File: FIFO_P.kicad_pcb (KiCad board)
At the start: 4 copper layers, 100 x 100 mm, 77 parts, among them J1 Vin +, J2 Vin -, J3 ICLK, J4 Vout, J5 Jack-DC, M3 MountingHole_3.2mm_M3_ISO14580, M4 MountingHole_4.3mm_M4_Pad_Via, SW1 Rotary_Encoder_61C, U1 SN74LVC2G157_MUX_TI, U10 AD7840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

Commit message: Fixed FIFO pin
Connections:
- U5 pad 13: GND -> (no net)
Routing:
- net (no net): track 0.00 -> 8.72 mm
- net GND: track 79.1 -> 77.0 mm, vias 11 -> 10
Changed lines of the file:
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@@
     (thickness 1.6)
     (drawings 116)
-    (tracks 1157)
+    (tracks 1160)
     (zones 0)
     (modules 77)
@@
     (mod_text_size 1 1)
     (mod_text_width 0.15)
-    (pad_size 3 3)
-    (pad_drill 1.52)
+    (pad_size 2.25 0.55)
+    (pad_drill 0)
     (pad_to_mask_clearance 0)
     (aux_axis_origin 0 0)
@@
     (pad 12 smd roundrect (at -8.05 2.8 270) (size 2.25 0.55) (layers F.Cu F.Paste F.Mask) (roundrect_rratio 0.25)
       (net 33 "Net-(U3-Pad20)"))
-    (pad 13 smd roundrect (at -8.05 3.6 270) (size 2.25 0.55) (layers F.Cu F.Paste F.Mask) (roundrect_rratio 0.25)
-      (net 88 GND))
+    (pad 13 smd roundrect (at -8.05 3.6 270) (size 2.25 0.55) (layers F.Cu F.Paste F.Mask) (roundrect_rratio 0.25))
     (pad 14 smd roundrect (at -8.05 4.4 270) (size 2.25 0.55) (layers F.Cu F.Paste F.Mask) (roundrect_rratio 0.25)
       (net 36 "Net-(U3-Pad17)"))
@@
   (gr_line (start 149.5 49.5) (end 149.5 149.5) (layer Edge.Cuts) (width 0.1))
   (gr_line (start 49.5 49.5) (end 149.5 49.5) (layer Edge.Cuts) (width 0.1))
+  (segment (start 113.1318 82.0414) (end 112.95001 82.22319) (width 0.25) (layer F.Cu) (net 0))
+  (segment (start 114.2568 82.0414) (end 113.1318 82.0414) (width 0.25) (layer F.Cu) (net 0))
+  (segment (start 112.95001 82.22319) (end 112.95001 86.45001) (width 0.25) (layer F.Cu) (net 0))
+  (segment (start 112.95001 86.45001) (end 114 87.5) (width 0.25) (layer F.Cu) (net 0))
+  (segment (start 114 87.5) (end 114 89.125) (width 0.25) (layer F.Cu) (net 0))
   (segment (start 115.3818 72.2914) (end 116.75 70.9232) (width 0.25) (layer F.Cu) (net 1))
   (segment (start 114.2568 72.2914) (end 115.3818 72.2914) (width 0.25) (layer F.Cu) (net 1))
@@
   (segment (start 114.8 87.387538) (end 114.8 87.9) (width 0.25) (layer F.Cu) (net 33))
   (segment (start 116.756064 82.799934) (end 115.415 84.140998) (width 0.25) (layer F.Cu) (net 33))
-  (segment (start 114.2568 80.0914) (end 113.1318 80.0914) (width 0.25) (layer F.Cu) (net 34))
-  (segment (start 111.849978 87.650022) (end 111.6 87.9) (width 0.25) (layer F.Cu) (net 34))
   (segment (start 111.6 87.9) (end 111.6 89.125) (width 0.25) (layer F.Cu) (net 34))
-  (segment (start 111.849978 81.373222) (end 111.849978 87.650022) (width 0.25) (layer F.Cu) (net 34))
-  (segment (start 113.1318 80.0914) (end 111.849978 81.373222) (width 0.25) (layer F.Cu) (net 34))
-  (segment (start 112.299989 87.799989) (end 112.299989 81.573211) (width 0.25) (layer F.Cu) (net 35))
-  (segment (start 112.299989 81.573211) (end 113.1318 80.7414) (width 0.25) (layer F.Cu) (net 35))
+  (segment (start 114.2568 80.0914) (end 113.1318 80.0914) (width 0.25) (layer F.Cu) (net 34))
+  (segment (start 111.599978 87.899978) (end 111.6 87.9) (width 0.25) (layer F.Cu) (net 34))
+  (segment (start 111.599978 81.623222) (end 111.599978 87.899978) (width 0.25) (layer F.Cu) (net 34))
+  (segment (start 113.1318 80.0914) (end 111.599978 81.623222) (width 0.25) (layer F.Cu) (net 34))
   (segment (start 113.1318 80.7414) (end 114.2568 80.7414) (width 0.25) (layer F.Cu) (net 35))
-  (segment (start 112.4 87.9) (end 112.299989 87.799989) (width 0.25) (layer F.Cu) (net 35))
-  (segment (start 112.4 89.125) (end 112.4 87.9) (width 0.25) (layer F.Cu) (net 35))
-  (segment (start 112.75 81.7732) (end 112.75 87.45) (width 0.25) (layer F.Cu) (net 36))
-  (segment (start 113.1318 81.3914) (end 112.75 81.7732) (width 0.25) (layer F.Cu) (net 36))
-  (segment (start 114.2568 81.3914) (end 113.1318 81.3914) (width 0.25) (layer F.Cu) (net 36))
-  (segment (start 112.75 87.45) (end 113.2 87.9) (width 0.25) (layer F.Cu) (net 36))
+  (segment (start 112.4 87.736411) (end 112.049989 87.3864) (width 0.25) (layer F.Cu) (net 35))
+  (segment (start 112.049989 81.823211) (end 113.1318 80.7414) (width 0.25) (layer F.Cu) (net 35))
+  (segment (start 112.4 89.125) (end 112.4 87.736411) (width 0.25) (layer F.Cu) (net 35))
+  (segment (start 112.049989 87.3864) (end 112.049989 81.823211) (width 0.25) (layer F.Cu) (net 35))
   (segment (start 113.2 87.9) (end 113.2 89.125) (width 0.25) (layer F.Cu) (net 36))
-  (segment (start 111.399967 87.100035) (end 109.55 88.950002) (width 0.25) (layer F.Cu) (net 37))
-  (segment (start 114.2568 79.4414) (end 113.1318 79.4414) (width 0.25) (layer F.Cu) (net 37))
-  (segment (start 113.1318 79.4414) (end 111.399967 81.173233) (width 0.25) (layer F.Cu) (net 37))
-  (segment (start 111.399967 81.173233) (end 111.399967 87.100035) (width 0.25) (layer F.Cu) (net 37))
+  (segment (start 112.5 87.2) (end 113.2 87.9) (width 0.25) (layer F.Cu) (net 36))
+  (segment (start 112.5 82.0232) (end 112.5 87.2) (width 0.25) (layer F.Cu) (net 36))
+  (segment (start 114.2568 81.3914) (end 113.1318 81.3914) (width 0.25) (layer F.Cu) (net 36))
+  (segment (start 113.1318 81.3914) (end 112.5 82.0232) (width 0.25) (layer F.Cu) (net 36))
   (segment (start 109.55 88.950002) (end 109.55 90.8) (width 0.25) (layer F.Cu) (net 37))
   (segment (start 109.55 90.8) (end 109.55 91.175) (width 0.25) (layer F.Cu) (net 37))
+  (segment (start 111.149967 87.350035) (end 109.55 88.950002) (width 0.25) (layer F.Cu) (net 37))
+  (segment (start 111.149967 81.423233) (end 111.149967 87.350035) (width 0.25) (layer F.Cu) (net 37))
+  (segment (start 114.2568 79.4414) (end 113.1318 79.4414) (width 0.25) (layer F.Cu) (net 37))
+  (segment (start 113.1318 79.4414) (end 111.149967 81.423233) (width 0.25) (layer F.Cu) (net 37))
   (segment (start 108.325 91.975) (end 109.55 91.975) (width 0.25) (layer F.Cu) (net 38))
   (segment (start 107.765 91.415) (end 108.325 91.975) (width 0.25) (layer F.Cu) (net 38))
   (segment (start 107.765 90.098591) (end 107.765 91.415) (width 0.25) (layer F.Cu) (net 38))
-  (segment (start 110.949956 86.913635) (end 107.765 90.098591) (width 0.25) (layer F.Cu) (net 38))
-  (segment (start 110.949956 80.973244) (end 110.949956 86.913635) (width 0.25) (layer F.Cu) (net 38))
-  (segment (start 113.1318 78.7914) (end 110.949956 80.973244) (width 0.25) (layer F.Cu) (net 38))
+  (segment (start 110.699956 87.163635) (end 107.765 90.098591) (width 0.25) (layer F.Cu) (net 38))
+  (segment (start 113.1318 78.7914) (end 110.699956 81.223244) (width 0.25) (layer F.Cu) (net 38))
   (segment (start 114.2568 78.7914) (end 113.1318 78.7914) (width 0.25) (layer F.Cu) (net 38))
-  (segment (start 110.499945 80.773255) (end 110.499945 86.727235) (width 0.25) (layer F.Cu) (net 39))
+  (segment (start 110.699956 81.223244) (end 110.699956 87.163635) (width 0.25) (layer F.Cu) (net 38))
+  (segment (start 108.247589 92.775) (end 108.325 92.775) (width 0.25) (layer F.Cu) (net 39))
   (segment (start 114.2568 78.1414) (end 113.1318 78.1414) (width 0.25) (layer F.Cu) (net 39))
-  (segment (start 110.499945 86.727235) (end 107.314989 89.912191) (width 0.25) (layer F.Cu) (net 39))
   (segment (start 107.314989 89.912191) (end 107.314989 91.8424) (width 0.25) (layer F.Cu) (net 39))
-  (segment (start 107.314989 91.8424) (end 108.247589 92.775) (width 0.25) (layer F.Cu) (net 39))
+  (segment (start 110.249945 86.977235) (end 107.314989 89.912191) (width 0.25) (layer F.Cu) (net 39))
   (segment (start 108.325 92.775) (end 109.55 92.775) (width 0.25) (layer F.Cu) (net 39))
-  (segment (start 108.247589 92.775) (end 108.325 92.775) (width 0.25) (layer F.Cu) (net 39))
-  (segment (start 113.1318 78.1414) (end 110.499945 80.773255) (width 0.25) (layer F.Cu) (net 39))
+  (segment (start 113.1318 78.1414) (end 110.249945 81.023255) (width 0.25) (layer F.Cu) (net 39))
+  (segment (start 110.249945 81.023255) (end 110.249945 86.977235) (width 0.25) (layer F.Cu) (net 39))
+  (segment (start 107.314989 91.8424) (end 108.247589 92.775) (width 0.25) (layer F.Cu) (net 39))
   (segment (start 126.125 97.575) (end 126.174999 97.624999) (width 0.25) (layer F.Cu) (net 40))
   (segment (start 125.275 97.575) (end 126.125 97.575) (width 0.25) (layer F.Cu) (net 40))
@@
   (segment (start 128.135 69.615) (end 129.25 68.5) (width 0.25) (layer F.Cu) (net 88))
   (segment (start 128.135 71.525) (end 128.135 69.615) (width 0.25) (layer F.Cu) (net 88))
-  (via (at 114 91.25) (size 0.8) (drill 0.4) (layers F.Cu B.Cu) (net 88))
   (via (at 111.5 96.75) (size 0.8) (drill 0.4) (layers F.Cu B.Cu) (net 88))
   (segment (start 73.25 88.75) (end 73.5 89) (width 0.5) (layer B.Cu) (net 88))
@@
   (segment (start 122.7 112.55) (end 122.7 111.555) (width 0.25) (layer B.Cu) (net 88))
   (segment (start 122.7 111.555) (end 123.16 111.095) (width 0.25) (layer B.Cu) (net 88))
-  (segment (start 114 89.125) (end 114 91.25) (width 0.25) (layer F.Cu) (net 88))
   (segment (start 120.4 87.271) (end 121.015 86.656) (width 0.25) (layer F.Cu) (net 88))
   (segment (start 120.4 89.125) (end 120.4 87.271) (width 0.25) (layer F.Cu) (net 88))

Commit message: Boop
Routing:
- net GND: track 77.0 -> 76.2 mm
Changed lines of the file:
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@@
     (thickness 1.6)
     (drawings 116)
-    (tracks 1160)
+    (tracks 1159)
     (zones 0)
     (modules 77)
@@
   (segment (start 74.75 94.75) (end 74.75 89) (width 1) (layer F.Cu) (net 88))
   (segment (start 74.75 83.08) (end 74.75 89) (width 1) (layer F.Cu) (net 88))
-  (segment (start 74.21 82.54) (end 74.75 83.08) (width 1) (layer F.Cu) (net 88))
   (segment (start 82.75 89) (end 82.75 91) (width 1) (layer F.Cu) (net 88))
   (segment (start 82.75 89) (end 82.75 87) (width 1) (layer F.Cu) (net 88))

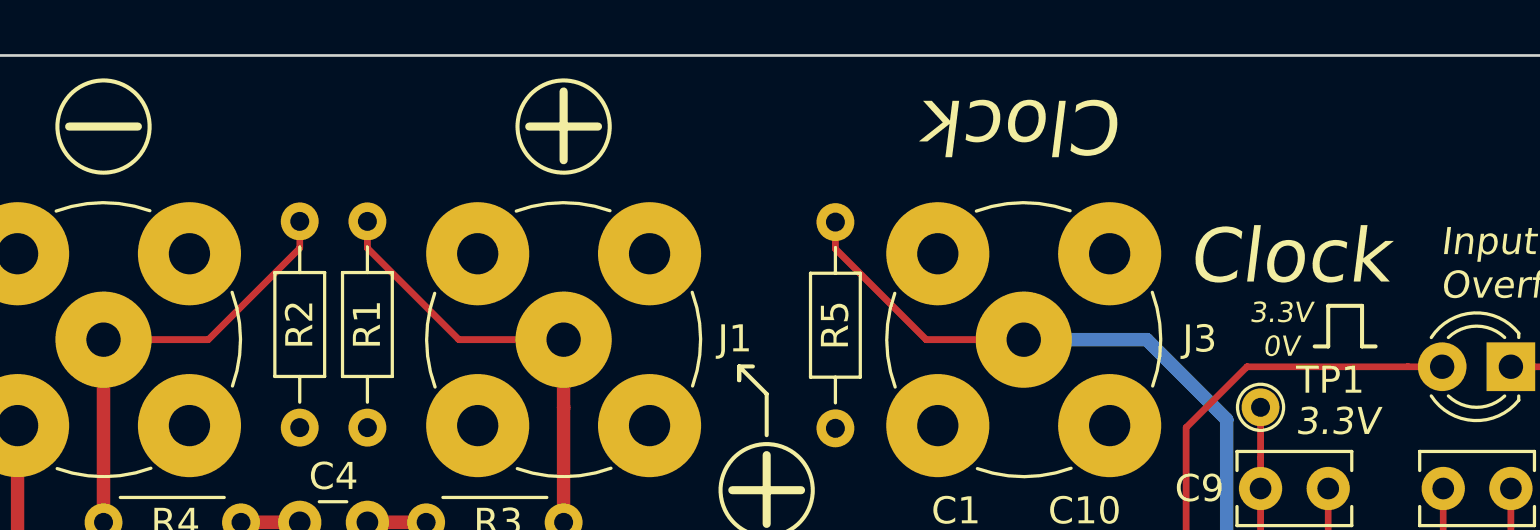
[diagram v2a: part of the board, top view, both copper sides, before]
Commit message: Cleaned up input limit silkscreen
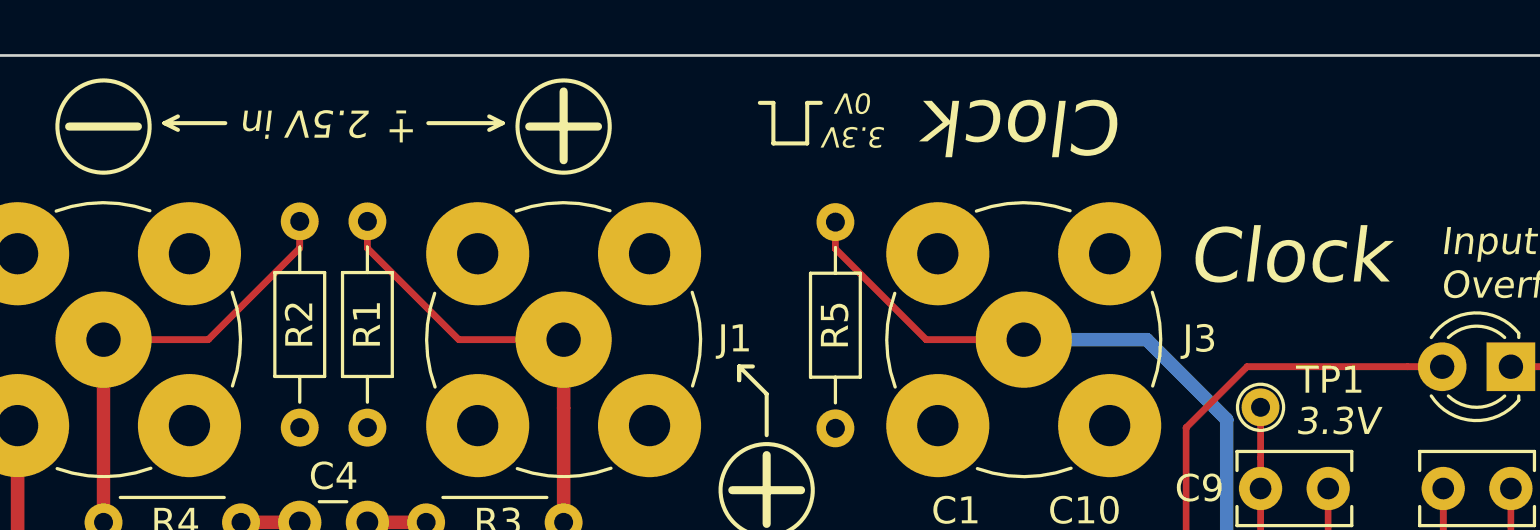
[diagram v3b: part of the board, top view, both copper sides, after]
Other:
- board text added: "+"
- board text added: "-"
- board text added: "2.5V in"
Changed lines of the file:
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@@
   (general
     (thickness 1.6)
-    (drawings 116)
+    (drawings 125)
     (tracks 1159)
     (zones 0)
@@
     )
   )
-  (gr_line (start 130.5 60.25) (end 131 60.25) (layer F.SilkS) (width 0.15))
-  (gr_line (start 130.5 58.75) (end 130.5 60.25) (layer F.SilkS) (width 0.15))
-  (gr_line (start 129.25 58.75) (end 130.5 58.75) (layer F.SilkS) (width 0.15))
-  (gr_line (start 129.25 60.25) (end 129.25 58.75) (layer F.SilkS) (width 0.15))
-  (gr_line (start 128.75 60.25) (end 129.25 60.25) (layer F.SilkS) (width 0.15))
-  (gr_text 0V (at 127.5 60.25) (layer F.SilkS)
+  (gr_line (start 98.75 52) (end 98.25 52.25) (layer F.SilkS) (width 0.15))
+  (gr_line (start 98.75 52) (end 98.25 51.75) (layer F.SilkS) (width 0.15))
+  (gr_line (start 86.25 52) (end 86.75 52.25) (layer F.SilkS) (width 0.15))
+  (gr_line (start 86.25 52) (end 86.75 51.75) (layer F.SilkS) (width 0.15))
+  (gr_line (start 88.5 52) (end 86.25 52) (layer F.SilkS) (width 0.15))
+  (gr_line (start 98.75 52) (end 96 52) (layer F.SilkS) (width 0.15))
+  (gr_text - (at 95 51.5) (layer F.SilkS)
+    (effects (font (size 1 1) (thickness 0.15)))
+  )
+  (gr_text + (at 95 52.25) (layer F.SilkS)
+    (effects (font (size 1 1) (thickness 0.15)))
+  )
+  (gr_text "2.5V in" (at 91.5 52 180) (layer F.SilkS)
+    (effects (font (size 1 1) (thickness 0.15) italic))
+  )
+  (gr_line (start 108.75 51.25) (end 108.25 51.25) (layer F.SilkS) (width 0.15))
+  (gr_line (start 108.75 52.75) (end 108.75 51.25) (layer F.SilkS) (width 0.15))
+  (gr_line (start 110 52.75) (end 108.75 52.75) (layer F.SilkS) (width 0.15))
+  (gr_line (start 110 51.25) (end 110 52.75) (layer F.SilkS) (width 0.15))
+  (gr_line (start 110.5 51.25) (end 110 51.25) (layer F.SilkS) (width 0.15))
+  (gr_text 0V (at 111.75 51.25 180) (layer F.SilkS)
     (effects (font (size 0.75 0.75) (thickness 0.125) italic))
   )
-  (gr_text 3.3V (at 127.5 59) (layer F.SilkS)
+  (gr_text 3.3V (at 111.75 52.5 180) (layer F.SilkS)
     (effects (font (size 0.75 0.75) (thickness 0.125) italic))
   )

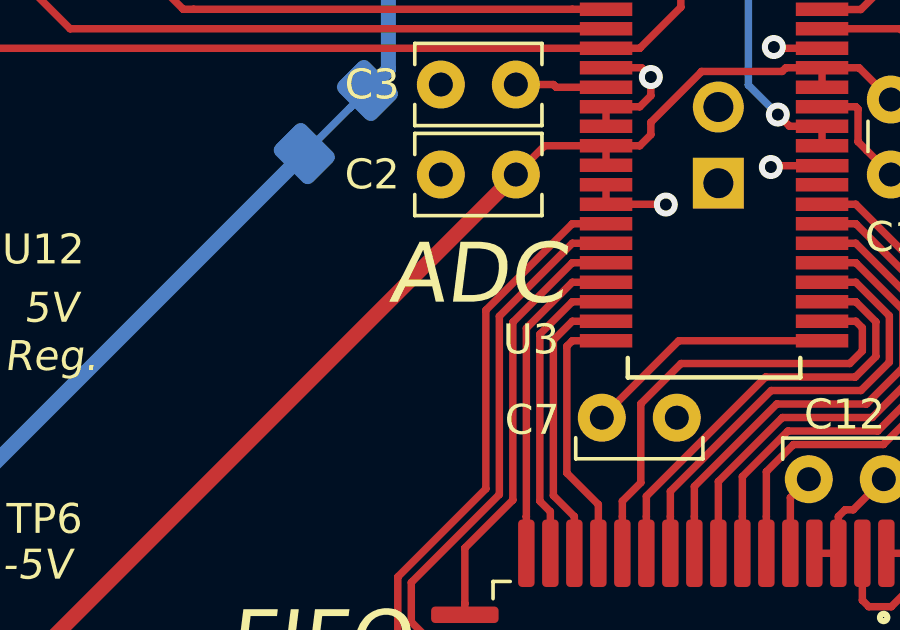
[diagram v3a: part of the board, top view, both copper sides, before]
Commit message: Add ADC specs
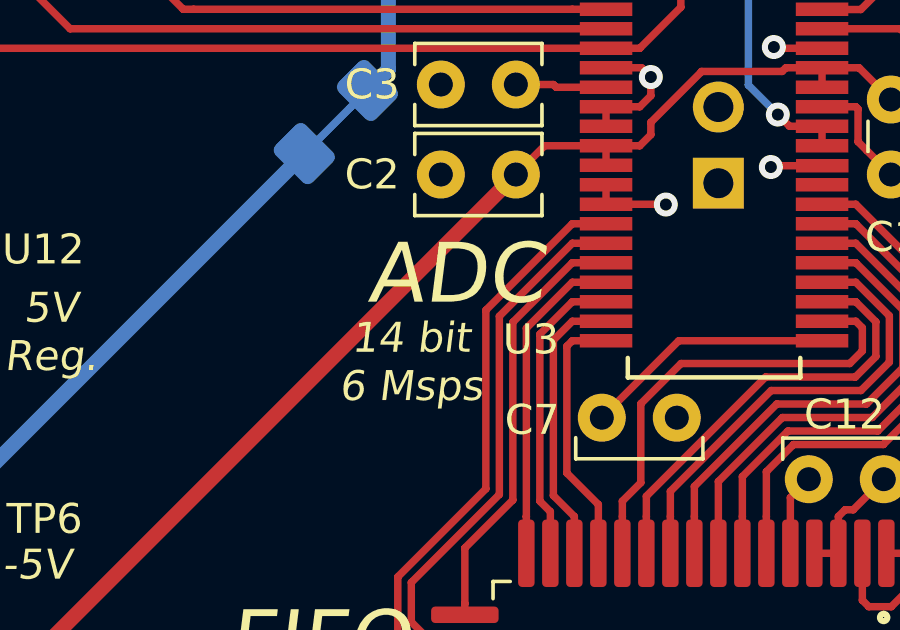
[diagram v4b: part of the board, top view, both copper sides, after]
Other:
- board text added: "14 bit 6 Msps"
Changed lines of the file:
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@@
   (general
     (thickness 1.6)
-    (drawings 125)
+    (drawings 126)
     (tracks 1159)
     (zones 0)
@@
     )
   )
+  (gr_text "14 bit\n6 Msps" (at 107.75 82.75) (layer F.SilkS)
+    (effects (font (size 1 1) (thickness 0.15) italic))
+  )
   (gr_line (start 98.75 52) (end 98.25 52.25) (layer F.SilkS) (width 0.15))
   (gr_line (start 98.75 52) (end 98.25 51.75) (layer F.SilkS) (width 0.15))
@@
     (effects (font (size 2 2) (thickness 0.15) italic))
   )
-  (gr_text ADC (at 109.96 79.815) (layer F.SilkS)
+  (gr_text ADC (at 109.25 79.815) (layer F.SilkS)
     (effects (font (size 2 2) (thickness 0.15) italic))
   )
